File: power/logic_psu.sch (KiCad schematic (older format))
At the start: 36 parts, among them J10 B3_Wago, J6 B3_Wago, J7 B3_Wago, J8 B3_Wago, J9 B3_Wago, Q4 ZXMP7A17G, U6 TPS40200D

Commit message: Updated power board for KiCAD 5
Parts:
- C1, C2, C45: symbol CP -> matemat_power-rescue:CP
- C46, C47, C49, C50, C51, C52, C53, C54, C55: symbol C -> matemat_power-rescue:C
- D1, D2, D3, D4, D5, D7, D8: symbol DIODE -> matemat_power-rescue:DIODE
- F3: symbol FUSE -> matemat_power-rescue:FUSE
- J10, J6, J7, J8, J9: symbol CONN_2 -> matemat_power-rescue:CONN_2
- L3: symbol INDUCTOR -> matemat_power-rescue:INDUCTOR
- Q4: symbol MOS_P_GDS -> matemat_power-rescue:MOS_P_GDS
- R33, R34, R36, R37, R38, R41, R42, R43: symbol R -> matemat_power-rescue:R
- U6: symbol TPS40200 -> matemat_power-rescue:TPS40200
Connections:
- wire segments 86 -> 122

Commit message: Recreated rescue library
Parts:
- C1, C2, C45: symbol matemat_power-rescue:CP -> matemat_power-rescue:CP-matemat_power-rescue
- C46, C47, C49, C50, C51, C52, C53, C54, C55: symbol matemat_power-rescue:C -> matemat_power-rescue:C-matemat_power-rescue
- D1, D2, D3, D4, D5, D7, D8: symbol matemat_power-rescue:DIODE -> matemat_power-rescue:DIODE-matemat_power-rescue
- F3: symbol matemat_power-rescue:FUSE -> matemat_power-rescue:FUSE-matemat_power-rescue
- J10, J6, J7, J8, J9: symbol matemat_power-rescue:CONN_2 -> matemat_power-rescue:CONN_2-matemat_power-rescue
- L3: symbol matemat_power-rescue:INDUCTOR -> matemat_power-rescue:INDUCTOR-matemat_power-rescue
- Q4: symbol matemat_power-rescue:MOS_P_GDS -> matemat_power-rescue:MOS_P_GDS-matemat_power-rescue
- R33, R34, R36, R37, R38, R41, R42, R43: symbol matemat_power-rescue:R -> matemat_power-rescue:R-matemat_power-rescue
- U6: symbol matemat_power-rescue:TPS40200 -> matemat_power-rescue:TPS40200-matemat_power-rescue

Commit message: Cleaned up schematics and removed obsolete parts
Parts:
- C1, C2, C45: footprint C2V10 -> Capacitor_THT:CP_Radial_D10.0mm_P5.00mm; symbol matemat_power-rescue:CP-matemat_power-rescue -> Device:CP
- C46, C47, C49, C50, C51, C52, C53, C54, C55: footprint SM0805 -> Capacitor_SMD:C_0805_2012Metric_Pad1.18x1.45mm_HandSolder; symbol matemat_power-rescue:C-matemat_power-rescue -> Device:C
- D1, D2, D3, D4: footprint DO214 -> Diode_SMD:D_SMA_Handsoldering; symbol matemat_power-rescue:DIODE-matemat_power-rescue -> Device:D_Schottky
- D5, D7, D8: footprint DO214 -> Diode_SMD:D_SMA_Handsoldering; symbol matemat_power-rescue:DIODE-matemat_power-rescue -> Device:D
- F3: footprint FUSE5-20 -> Fuse:Fuseholder_Cylinder-5x20mm_Schurter_0031_8201_Horizontal_Open; symbol matemat_power-rescue:FUSE-matemat_power-rescue -> Device:Fuse
- J10, J6, J7, J8, J9: footprint Bornier_B2_Wago -> TerminalBlock_WAGO:TerminalBlock_WAGO_236-102_1x02_P5.00mm_45Degree; symbol matemat_power-rescue:CONN_2-matemat_power-rescue -> Connector_Generic:Conn_01x02
- L3: footprint ALTNC -> Inductor_THT:L_Toroid_Vertical_L22.4mm_W10.2mm_P7.90mm_Vishay_TJ4; symbol matemat_power-rescue:INDUCTOR-matemat_power-rescue -> Device:L
- Q4: footprint -SOT223-3 -> Package_TO_SOT_SMD:SOT-223-3_TabPin2; symbol matemat_power-rescue:MOS_P_GDS-matemat_power-rescue -> Device:Q_PMOS_GDS
- R33, R34, R36, R37, R38, R41, R42: footprint SM0805 -> Resistor_SMD:R_0805_2012Metric_Pad1.20x1.40mm_HandSolder; symbol matemat_power-rescue:R-matemat_power-rescue -> Device:R
- R43: footprint -R2010 -> Resistor_SMD:R_2010_5025Metric_Pad1.40x2.65mm_HandSolder; symbol matemat_power-rescue:R-matemat_power-rescue -> Device:R
- U6: footprint -SO-08 -> Package_SO:SOIC-8_3.9x4.9mm_P1.27mm; symbol matemat_power-rescue:TPS40200-matemat_power-rescue -> oni:TPS40200
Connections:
- net +5V is gone; now on net +12V: C2.1, C54.1, C55.1, J10.1 (Pin_1), J9.1 (Pin_1), L3.2, R37.2, R38.2
- net +12V: no longer C1.1, C45.1, C46.1, C53.1, D1.1 (A), D1.2 (K), D2.2 (K), D3.2 (K), F3.2, J7.1 (P1), J8.1 (P1), R36.1, R43.2, U6.8 (VDD)
- net GND: now also D2.2 (A), D5.2 (A), D7.2 (A), D8.2 (A); no longer D2.1 (A), D3.1 (A), D4.1 (A), D5.1 (A), D7.1 (A), D8.1 (A), J6.2 (PM)
- net at F3.1: now also D1.2 (A), D2.1 (K); no longer J6.1 (P1)
- new net: D5.1 (K), D7.1 (K), D8.1 (K), L3.1, Q4.2 (D)
- new net: D3.2 (A), D4.1 (K), J6.2 (Pin_2)
- new net: F3.2, J6.1 (Pin_1)
- new net +28V: C1.1, C45.1, C46.1, C53.1, D1.1 (K), D3.1 (K), J7.1 (Pin_1), J8.1 (Pin_1), R36.1, R43.2, U6.8 (VDD)
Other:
- moved on the sheet: D5, L3

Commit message: Updated PCB layout
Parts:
- removed J10, J8, J9: B3_Wago, TerminalBlock_WAGO:TerminalBlock_WAGO_236-102_1x02_P5.00mm_45Degree, symbol Connector_Generic:Conn_01x02
- J6: footprint TerminalBlock_WAGO:TerminalBlock_WAGO_236-102_1x02_P5.00mm_45Degree -> TerminalBlock_WAGO:TerminalBlock_WAGO_236-402_1x02_P5.00mm_45Degree
- J7: footprint TerminalBlock_WAGO:TerminalBlock_WAGO_236-102_1x02_P5.00mm_45Degree -> TerminalBlock_WAGO:TerminalBlock_WAGO_236-408_1x08_P5.00mm_45Degree; symbol Connector_Generic:Conn_01x02 -> Connector_Generic:Conn_01x08; Reference FAR 1283527 -> (none); prix 0,84 -> (none)
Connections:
- net +12V: now also J7.5 (Pin_5), J7.7 (Pin_7)
- net +28V: now also J7.3 (Pin_3)
- net GND: now also J7.4 (Pin_4), J7.6 (Pin_6), J7.8 (Pin_8)
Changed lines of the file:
@@
-	1    0    0    -1
-$EndComp
-$Comp
-L Connector_Generic:Conn_01x02 J7
-U 1 1 50F5F1A5
-P 10650 1500
-AR Path="/50F5F1A5" Ref="J7"  Part="1"
-AR Path="/50FF13A8/50F5F1A5" Ref="J7"  Part="1"
-F 0 "J7" V 10600 1500 50  0000 C CNN
-F 1 "B3_Wago" V 10700 1500 40  0000 C CNN
-F 2 "TerminalBlock_WAGO:TerminalBlock_WAGO_236-102_1x02_P5.00mm_45Degree" H 10650 1500 60  0001 C CNN
-F 3 "" H 10650 1500 60  0001 C CNN
-F 4 "FAR 1283527" H 10650 1500 60  0001 C CNN "Reference"
-F 5 "0,84" H 10650 1500 60  0001 C CNN "prix"
-	1    10650 1500
-	1    0    0    -1
-$EndComp
-$Comp
-L Connector_Generic:Conn_01x02 J9
-U 1 1 50F5F1AD
-P 9450 1500
-AR Path="/50F5F1AD" Ref="J9"  Part="1"
-AR Path="/50FF13A8/50F5F1AD" Ref="J9"  Part="1"
-F 0 "J9" V 9400 1500 50  0000 C CNN
-F 1 "B3_Wago" V 9500 1500 40  0000 C CNN
-F 2 "TerminalBlock_WAGO:TerminalBlock_WAGO_236-102_1x02_P5.00mm_45Degree" H 9450 1500 60  0001 C CNN
-F 3 "" H 9450 1500 60  0001 C CNN
-F 4 "FAR 1283527" H 9450 1500 60  0001 C CNN "Reference"
-F 5 "0,84" H 9450 1500 60  0001 C CNN "prix"
-	1    9450 1500
 	1    0    0    -1
 $EndComp
@@
 	3350 2350 3350 2850
 Connection ~ 3350 2350
-Wire Wire Line
-	10250 1500 10450 1500
-Wire Wire Line
-	10450 1600 10250 1600
-Wire Wire Line
-	9050 1500 9250 1500
-$Comp
-L Connector_Generic:Conn_01x02 J8
-U 1 1 5105778D
-P 10650 1000
-AR Path="/5105778D" Ref="J8"  Part="1"
-AR Path="/50FF13A8/5105778D" Ref="J8"  Part="1"
-F 0 "J8" V 10600 1000 50  0000 C CNN
-F 1 "B3_Wago" V 10700 1000 40  0000 C CNN
-F 2 "TerminalBlock_WAGO:TerminalBlock_WAGO_236-102_1x02_P5.00mm_45Degree" H 10650 1000 60  0001 C CNN
-F 3 "" H 10650 1000 60  0001 C CNN
-F 4 "FAR 1283527" H 10650 1000 60  0001 C CNN "Reference"
-F 5 "0,84" H 10650 1000 60  0001 C CNN "prix"
-	1    10650 1000
-	1    0    0    -1
-$EndComp
-$Comp
-L Connector_Generic:Conn_01x02 J10
-U 1 1 51057795
-P 9450 1000
-AR Path="/51057795" Ref="J10"  Part="1"
-AR Path="/50FF13A8/51057795" Ref="J10"  Part="1"
-F 0 "J10" V 9400 1000 50  0000 C CNN
-F 1 "B3_Wago" V 9500 1000 40  0000 C CNN
-F 2 "TerminalBlock_WAGO:TerminalBlock_WAGO_236-102_1x02_P5.00mm_45Degree" H 9450 1000 60  0001 C CNN
-F 3 "" H 9450 1000 60  0001 C CNN
-F 4 "FAR 1283527" H 9450 1000 60  0001 C CNN "Reference"
-F 5 "0,84" H 9450 1000 60  0001 C CNN "prix"
-	1    9450 1000
-	1    0    0    -1
-$EndComp
-Wire Wire Line
-	10250 1000 10450 1000
-Wire Wire Line
-	10450 1100 10250 1100
-Wire Wire Line
-	9050 1000 9250 1000
-Wire Wire Line
-	9250 1100 9050 1100
 Wire Wire Line
 	9850 3500 10700 3500
@@
 F 0 "J6" V 1150 2850 50  0000 C CNN
 F 1 "B3_Wago" V 1250 2850 40  0000 C CNN
-F 2 "TerminalBlock_WAGO:TerminalBlock_WAGO_236-102_1x02_P5.00mm_45Degree" H 1200 2850 60  0001 C CNN
+F 2 "TerminalBlock_WAGO:TerminalBlock_WAGO_236-402_1x02_P5.00mm_45Degree" H 1200 2850 60  0001 C CNN
 F 3 "" H 1200 2850 60  0001 C CNN
 F 4 "FAR 1283527" H 1200 2850 60  0001 C CNN "Reference"
@@
 	1    0    0    -1
 $EndComp
+Connection ~ 9500 1750
+Wire Wire Line
+	9500 1750 9700 1750
+Wire Wire Line
+	9500 1950 9700 1950
+Wire Wire Line
+	9500 1750 9500 1950
 $Comp
 L power:+12V #PWR0175
-U 1 1 6021237C
-P 9050 1000
-F 0 "#PWR0175" H 9050 850 50  0001 C CNN
-F 1 "+12V" H 9065 1173 50  0000 C CNN
-F 2 "" H 9050 1000 50  0001 C CNN
-F 3 "" H 9050 1000 50  0001 C CNN
-	1    9050 1000
-	1    0    0    -1
-$EndComp
-$Comp
-L power:+12V #PWR0176
-U 1 1 602127F5
-P 9050 1500
-F 0 "#PWR0176" H 9050 1350 50  0001 C CNN
-F 1 "+12V" H 9065 1673 50  0000 C CNN
-F 2 "" H 9050 1500 50  0001 C CNN
-F 3 "" H 9050 1500 50  0001 C CNN
-	1    9050 1500
-	1    0    0    -1
-$EndComp
-$Comp
-L power:+28V #PWR0177
-U 1 1 602130F0
-P 10250 1000
-F 0 "#PWR0177" H 10250 850 50  0001 C CNN
-F 1 "+28V" H 10265 1173 50  0000 C CNN
-F 2 "" H 10500 1050 50  0001 C CNN
-F 3 "" H 10500 1050 50  0001 C CNN
-	1    10250 1000
+U 1 1 60094D63
+P 9500 1750
+F 0 "#PWR0175" H 9500 1600 50  0001 C CNN
+F 1 "+12V" H 9515 1923 50  0000 C CNN
+F 2 "" H 9500 1750 50  0001 C CNN
+F 3 "" H 9500 1750 50  0001 C CNN
+	1    9500 1750
+	1    0    0    -1
+$EndComp
+Wire Wire Line
+	9600 2050 9600 1850
+Connection ~ 9600 2050
+Wire Wire Line
+	9600 2050 9700 2050
+Wire Wire Line
+	9600 1850 9600 1650
+Connection ~ 9600 1850
+Wire Wire Line
+	9600 1850 9700 1850
+Wire Wire Line
+	9600 1650 9600 1450
+Connection ~ 9600 1650
+Wire Wire Line
+	9600 1650 9700 1650
+Connection ~ 9500 1350
+Wire Wire Line
+	9500 1550 9700 1550
+Wire Wire Line
+	9500 1350 9500 1550
+Wire Wire Line
+	9600 2150 9600 2050
+$Comp
+L power:GND #PWR0181
+U 1 1 602286BD
+P 9600 2150
+F 0 "#PWR0181" H 9600 1900 50  0001 C CNN
+F 1 "GND" H 9605 1977 50  0000 C CNN
+F 2 "" H 9600 2150 50  0001 C CNN
+F 3 "" H 9600 2150 50  0001 C CNN
+	1    9600 2150
 	1    0    0    -1
 $EndComp
@@
 L power:+28V #PWR0178
 U 1 1 602132D1
-P 10250 1500
-F 0 "#PWR0178" H 10250 1350 50  0001 C CNN
-F 1 "+28V" H 10265 1673 50  0000 C CNN
-F 2 "" H 10500 1550 50  0001 C CNN
-F 3 "" H 10500 1550 50  0001 C CNN
-	1    10250 1500
-	1    0    0    -1
-$EndComp
-Wire Wire Line
-	9250 1600 9050 1600
-$Comp
-L power:GND #PWR0179
-U 1 1 60227F7D
-P 9050 1100
-F 0 "#PWR0179" H 9050 850 50  0001 C CNN
-F 1 "GND" H 9055 927 50  0000 C CNN
-F 2 "" H 9050 1100 50  0001 C CNN
-F 3 "" H 9050 1100 50  0001 C CNN
-	1    9050 1100
-	1    0    0    -1
-$EndComp
-$Comp
-L power:GND #PWR0180
-U 1 1 602282F0
-P 10250 1100
-F 0 "#PWR0180" H 10250 850 50  0001 C CNN
-F 1 "GND" H 10255 927 50  0000 C CNN
-F 2 "" H 10250 1100 50  0001 C CNN
-F 3 "" H 10250 1100 50  0001 C CNN
-	1    10250 1100
-	1    0    0    -1
-$EndComp
-$Comp
-L power:GND #PWR0181
-U 1 1 602286BD
-P 10250 1600
-F 0 "#PWR0181" H 10250 1350 50  0001 C CNN
-F 1 "GND" H 10255 1427 50  0000 C CNN
-F 2 "" H 10250 1600 50  0001 C CNN
-F 3 "" H 10250 1600 50  0001 C CNN
-	1    10250 1600
-	1    0    0    -1
-$EndComp
-$Comp
-L power:GND #PWR0182
-U 1 1 6022897E
-P 9050 1600
-F 0 "#PWR0182" H 9050 1350 50  0001 C CNN
-F 1 "GND" H 9055 1427 50  0000 C CNN
-F 2 "" H 9050 1600 50  0001 C CNN
-F 3 "" H 9050 1600 50  0001 C CNN
-	1    9050 1600
-	1    0    0    -1
-$EndComp
+P 9500 1350
+F 0 "#PWR0178" H 9500 1200 50  0001 C CNN
+F 1 "+28V" H 9515 1523 50  0000 C CNN
+F 2 "" H 9750 1400 50  0001 C CNN
+F 3 "" H 9750 1400 50  0001 C CNN
+	1    9500 1350
+	1    0    0    -1
+$EndComp
+Wire Wire Line
+	9700 1450 9600 1450
+Wire Wire Line
+	9500 1350 9700 1350
+$Comp
+L Connector_Generic:Conn_01x08 J7
+U 1 1 50F5F1A5
+P 9900 1650
+AR Path="/50F5F1A5" Ref="J7"  Part="1"
+AR Path="/50FF13A8/50F5F1A5" Ref="J7"  Part="1"
+F 0 "J7" H 9900 2050 50  0000 C CNN
+F 1 "B3_Wago" H 9900 1150 50  0000 C CNN
+F 2 "TerminalBlock_WAGO:TerminalBlock_WAGO_236-408_1x08_P5.00mm_45Degree" H 9900 1650 50  0001 C CNN
+F 3 "" H 9900 1650 50  0001 C CNN
+	1    9900 1650
+	1    0    0    -1
+$EndComp

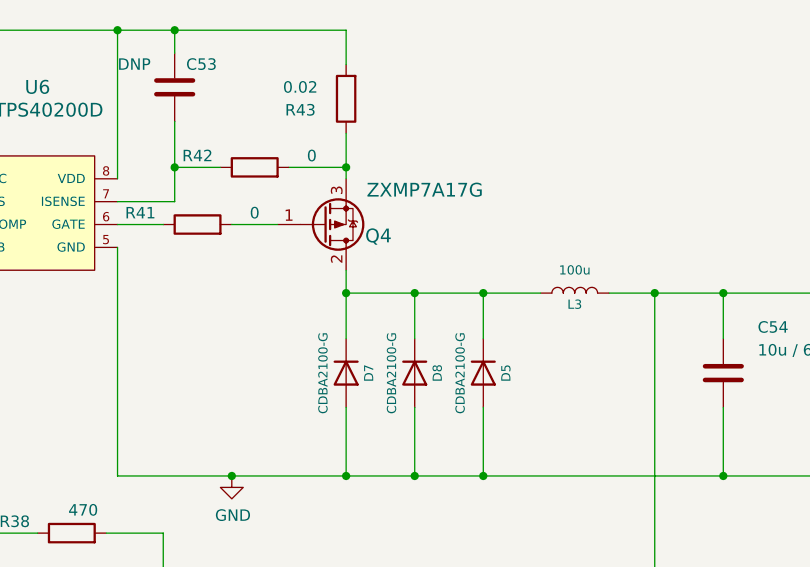
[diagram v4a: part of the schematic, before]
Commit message: Replaced power board diode pad layouts
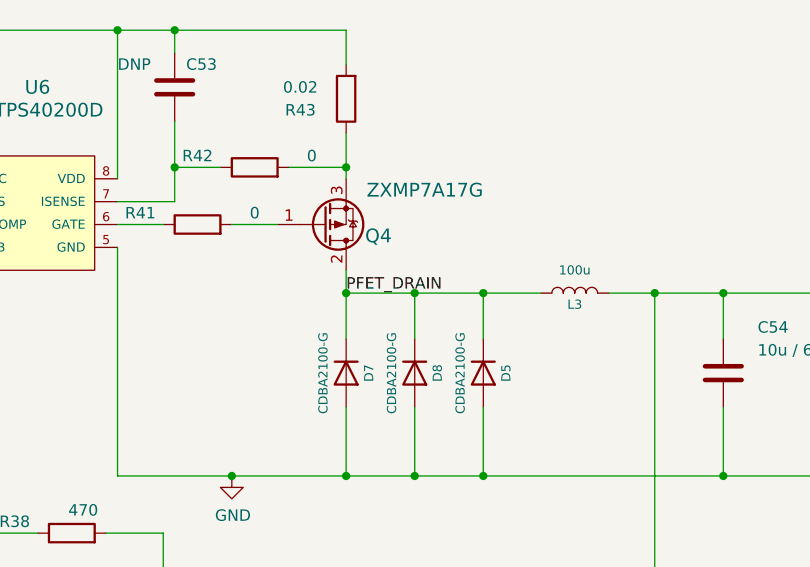
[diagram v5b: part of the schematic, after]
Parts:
- D1, D2, D3, D4, D5, D7, D8: footprint Diode_SMD:D_SMA_Handsoldering -> Diode_SMD:D_SMA
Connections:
- net PFET_DRAIN: now reaches D5.1 (K), D7.1 (K), D8.1 (K), L3.1, Q4.2 (D)
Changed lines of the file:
@@
 F 0 "D7" H 7450 3950 40  0000 C CNN
 F 1 "CDBA2100-G" H 7450 3750 40  0000 C CNN
-F 2 "Diode_SMD:D_SMA_Handsoldering" H 7450 3850 60  0001 C CNN
+F 2 "Diode_SMD:D_SMA" H 7450 3850 60  0001 C CNN
 F 3 "" H 7450 3850 60  0001 C CNN
 F 4 "RS 636-5088" H 7450 3850 60  0001 C CNN "Reference"
@@
 F 0 "D8" H 7750 3950 40  0000 C CNN
 F 1 "CDBA2100-G" H 7750 3750 40  0000 C CNN
-F 2 "Diode_SMD:D_SMA_Handsoldering" H 7750 3850 60  0001 C CNN
+F 2 "Diode_SMD:D_SMA" H 7750 3850 60  0001 C CNN
 F 3 "" H 7750 3850 60  0001 C CNN
 F 4 "RS 636-5088" H 7750 3850 60  0001 C CNN "Reference"
@@
 F 0 "D5" H 8050 3950 40  0000 C CNN
 F 1 "CDBA2100-G" H 8050 3750 40  0000 C CNN
-F 2 "Diode_SMD:D_SMA_Handsoldering" H 8050 3850 60  0001 C CNN
+F 2 "Diode_SMD:D_SMA" H 8050 3850 60  0001 C CNN
 F 3 "" H 8050 3850 60  0001 C CNN
 F 4 "RS 636-5088" H 8050 3850 60  0001 C CNN "Reference"
@@
 F 0 "D1" H 2200 2700 40  0000 C CNN
 F 1 "CDBA2100-G" H 2200 2500 40  0000 C CNN
-F 2 "Diode_SMD:D_SMA_Handsoldering" H 2200 2600 60  0001 C CNN
+F 2 "Diode_SMD:D_SMA" H 2200 2600 60  0001 C CNN
 F 3 "" H 2200 2600 60  0001 C CNN
 F 4 "RS 636-5088" H 2200 2600 60  0001 C CNN "Reference"
@@
 F 0 "D2" H 2200 3300 40  0000 C CNN
 F 1 "CDBA2100-G" H 2200 3100 40  0000 C CNN
-F 2 "Diode_SMD:D_SMA_Handsoldering" H 2200 3200 60  0001 C CNN
+F 2 "Diode_SMD:D_SMA" H 2200 3200 60  0001 C CNN
 F 3 "" H 2200 3200 60  0001 C CNN
 F 4 "RS 636-5088" H 2200 3200 60  0001 C CNN "Reference"
@@
 F 0 "D3" H 2700 2700 40  0000 C CNN
 F 1 "CDBA2100-G" H 2700 2500 40  0000 C CNN
-F 2 "Diode_SMD:D_SMA_Handsoldering" H 2700 2600 60  0001 C CNN
+F 2 "Diode_SMD:D_SMA" H 2700 2600 60  0001 C CNN
 F 3 "" H 2700 2600 60  0001 C CNN
 F 4 "RS 636-5088" H 2700 2600 60  0001 C CNN "Reference"
@@
 F 0 "D4" H 2700 3300 40  0000 C CNN
 F 1 "CDBA2100-G" H 2700 3100 40  0000 C CNN
-F 2 "Diode_SMD:D_SMA_Handsoldering" H 2700 3200 60  0001 C CNN
+F 2 "Diode_SMD:D_SMA" H 2700 3200 60  0001 C CNN
 F 3 "" H 2700 3200 60  0001 C CNN
 F 4 "RS 636-5088" H 2700 3200 60  0001 C CNN "Reference"
@@
 	1    0    0    -1
 $EndComp
+Text Label 7450 3500 0    50   ~ 0
+PFET_DRAIN
 $EndSCHEMATC
